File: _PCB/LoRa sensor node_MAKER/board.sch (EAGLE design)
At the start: 25 parts

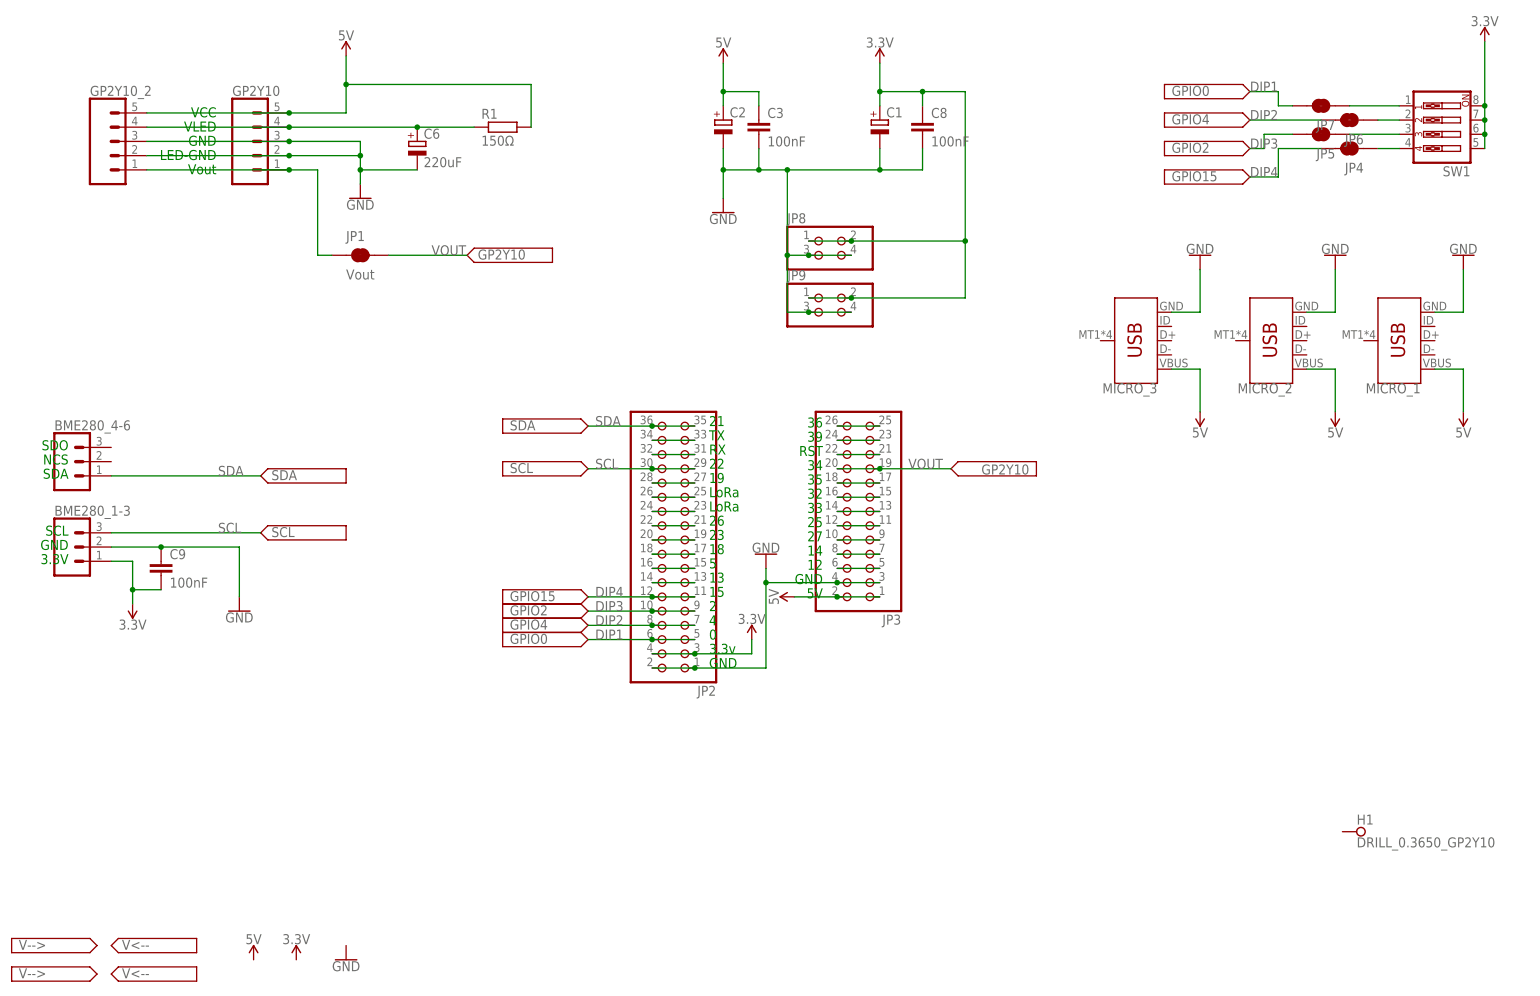
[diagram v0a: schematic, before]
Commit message: CH340E converter complete + LoRa sensor node
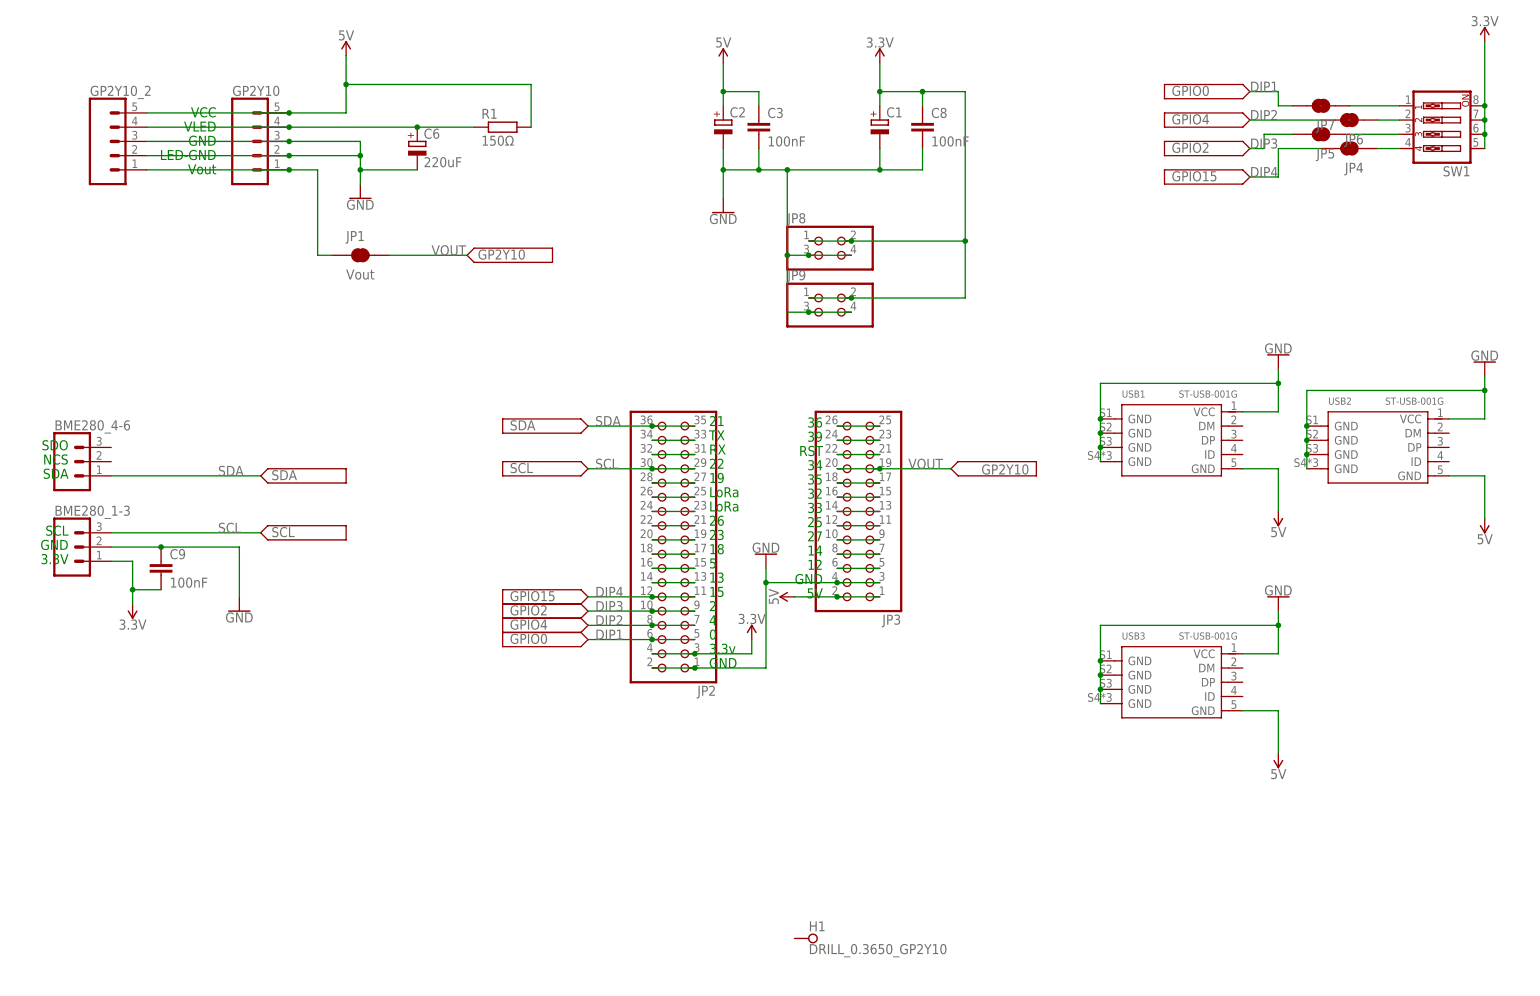
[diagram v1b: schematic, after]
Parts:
- removed MICRO_1, MICRO_2, MICRO_3: (no value), SparkFun-Connectors:USB_MICRO-B_SMT
- added USB1, USB2, USB3: ST-USB-001G, Seeed-Connector:MICRO-USB-SMD-B-WITHOUT-POST-W/P(ST-USB-001G)
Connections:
- net 5V: now also USB1.GND@5, USB2.GND@5, USB3.GND@5; no longer MICRO_1.VBUS, MICRO_2.VBUS, MICRO_3.VBUS
- net GND: now also USB1.GND@1, USB1.GND@2, USB1.GND@3, USB1.GND@4, USB1.VCC, USB2.GND@1, USB2.GND@2, USB2.GND@3, USB2.GND@4, USB2.VCC, USB3.GND@1, USB3.GND@2, USB3.GND@3, USB3.GND@4, USB3.VCC; no longer MICRO_1.GND, MICRO_2.GND, MICRO_3.GND
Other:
- moved on the sheet: H1

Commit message: error correciton
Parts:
- removed USB1: ST-USB-001G, Seeed-Connector:MICRO-USB-SMD-B-WITHOUT-POST-W/P(ST-USB-001G)
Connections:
- net 5V: no longer USB1.GND@5
- net GND: no longer USB1.GND@1, USB1.GND@2, USB1.GND@3, USB1.GND@4, USB1.VCC
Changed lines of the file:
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@@
 <setting verticaltext="up"/>
 </settings>
-<grid distance="50" unitdist="mil" unit="mil" style="lines" multiple="1" display="no" altdistance="0.01" altunitdist="inch" altunit="inch"/>
+<grid distance="0.1" unitdist="inch" unit="inch" style="lines" multiple="1" display="no" altdistance="0.01" altunitdist="inch" altunit="inch"/>
 <layers>
 <layer number="1" name="Top" color="4" fill="1" visible="no" active="no"/>
@@
 <part name="JP8" library="pinhead_v2" deviceset="PINHD-2X2" device="/OCT"/>
 <part name="JP9" library="pinhead_v2" deviceset="PINHD-2X2" device="/OCT"/>
-<part name="USB1" library="Seeed-Connector" library_urn="urn:adsk.eagle:library:478" deviceset="MICRO-USB-SMD-B-WITHOUT-POST-W/P(ST-USB-001G)" device="" package3d_urn="urn:adsk.eagle:package:33109/1" value="ST-USB-001G"/>
-<part name="SUPPLY17" library="SparkFun-PowerSymbols" library_urn="urn:adsk.eagle:library:530" deviceset="5V" device=""/>
-<part name="GND9" library="SparkFun-PowerSymbols" library_urn="urn:adsk.eagle:library:530" deviceset="GND" device=""/>
 <part name="USB2" library="Seeed-Connector" library_urn="urn:adsk.eagle:library:478" deviceset="MICRO-USB-SMD-B-WITHOUT-POST-W/P(ST-USB-001G)" device="" package3d_urn="urn:adsk.eagle:package:33109/1" value="ST-USB-001G"/>
 <part name="SUPPLY32" library="SparkFun-PowerSymbols" library_urn="urn:adsk.eagle:library:530" deviceset="5V" device=""/>
@@
 <attribute name="VALUE" x="146.05" y="120.65" size="1.778" layer="96"/>
 </instance>
-<instance part="USB1" gate="USB" x="214.63" y="102.87" smashed="yes">
-<attribute name="NAME" x="205.74" y="110.49" size="1.27" layer="95" ratio="10"/>
-<attribute name="VALUE" x="215.9" y="110.49" size="1.27" layer="95" ratio="10"/>
-</instance>
-<instance part="SUPPLY17" gate="G$1" x="233.68" y="90.17" smashed="yes" rot="R180">
-<attribute name="VALUE" x="233.68" y="87.376" size="1.778" layer="96" rot="R180" align="bottom-center"/>
-</instance>
-<instance part="GND9" gate="1" x="233.68" y="118.11" smashed="yes" rot="R180">
-<attribute name="VALUE" x="233.68" y="118.364" size="1.778" layer="96" rot="R180" align="top-center"/>
-</instance>
 <instance part="USB2" gate="USB" x="251.46" y="101.6" smashed="yes">
 <attribute name="NAME" x="242.57" y="109.22" size="1.27" layer="95" ratio="10"/>
@@
 </segment>
 <segment>
-<pinref part="GND9" gate="1" pin="GND"/>
-<wire x1="227.33" y1="107.95" x2="233.68" y2="107.95" width="0.1524" layer="91"/>
-<wire x1="233.68" y1="107.95" x2="233.68" y2="113.03" width="0.1524" layer="91"/>
-<pinref part="USB1" gate="USB" pin="VCC"/>
-<pinref part="USB1" gate="USB" pin="GND@4"/>
-<pinref part="USB1" gate="USB" pin="GND@3"/>
-<wire x1="233.68" y1="113.03" x2="233.68" y2="115.57" width="0.1524" layer="91"/>
-<wire x1="201.93" y1="99.06" x2="201.93" y2="101.6" width="0.1524" layer="91"/>
-<pinref part="USB1" gate="USB" pin="GND@2"/>
-<wire x1="201.93" y1="101.6" x2="201.93" y2="104.14" width="0.1524" layer="91"/>
-<junction x="201.93" y="101.6"/>
-<pinref part="USB1" gate="USB" pin="GND@1"/>
-<wire x1="201.93" y1="104.14" x2="201.93" y2="106.68" width="0.1524" layer="91"/>
-<junction x="201.93" y="104.14"/>
-<wire x1="201.93" y1="106.68" x2="201.93" y2="113.03" width="0.1524" layer="91"/>
-<wire x1="201.93" y1="113.03" x2="233.68" y2="113.03" width="0.1524" layer="91"/>
-<junction x="201.93" y="106.68"/>
-<junction x="233.68" y="113.03"/>
-</segment>
-<segment>
 <pinref part="GND10" gate="1" pin="GND"/>
 <wire x1="264.16" y1="106.68" x2="270.51" y2="106.68" width="0.1524" layer="91"/>
@@
 </segment>
 <segment>
-<pinref part="SUPPLY17" gate="G$1" pin="5V"/>
-<wire x1="227.33" y1="97.79" x2="233.68" y2="97.79" width="0.1524" layer="91"/>
-<wire x1="233.68" y1="97.79" x2="233.68" y2="90.17" width="0.1524" layer="91"/>
-<pinref part="USB1" gate="USB" pin="GND@5"/>
-</segment>
-<segment>

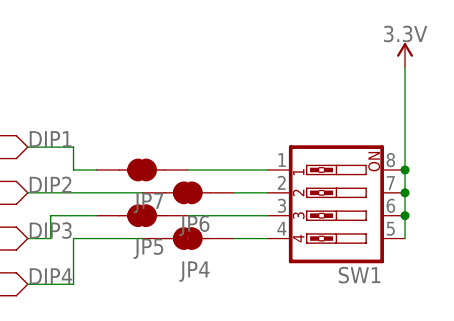
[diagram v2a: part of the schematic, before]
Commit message: LoRa sensor node PCB update
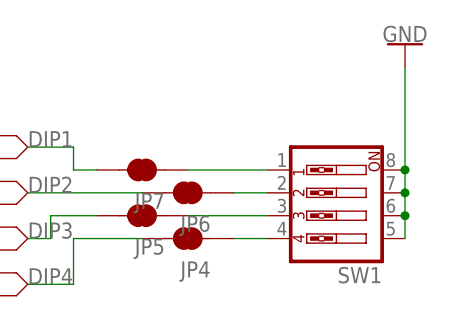
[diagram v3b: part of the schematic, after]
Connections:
- net 3.3V: no longer SW1.5, SW1.6, SW1.7, SW1.8
- net GND: now also SW1.5, SW1.6, SW1.7, SW1.8
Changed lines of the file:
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@@
 <setting verticaltext="up"/>
 </settings>
-<grid distance="0.1" unitdist="inch" unit="inch" style="lines" multiple="1" display="no" altdistance="0.01" altunitdist="inch" altunit="inch"/>
+<grid distance="0.05" unitdist="inch" unit="inch" style="lines" multiple="1" display="no" altdistance="0.01" altunitdist="inch" altunit="inch"/>
 <layers>
 <layer number="1" name="Top" color="4" fill="1" visible="no" active="no"/>
@@
 <part name="JP6" library="SparkFun-Jumpers" library_urn="urn:adsk.eagle:library:528" deviceset="JUMPER-SMT_2_NC_TRACE" device="_SILK" package3d_urn="urn:adsk.eagle:package:39281/1" value=""/>
 <part name="JP7" library="SparkFun-Jumpers" library_urn="urn:adsk.eagle:library:528" deviceset="JUMPER-SMT_2_NC_TRACE" device="_SILK" package3d_urn="urn:adsk.eagle:package:39281/1" value=""/>
-<part name="SUPPLY2" library="SparkFun-PowerSymbols" library_urn="urn:adsk.eagle:library:530" deviceset="3.3V" device=""/>
 <part name="SUPPLY18" library="supply2" library_urn="urn:adsk.eagle:library:372" deviceset="V--&gt;" device="" value="GPIO15"/>
 <part name="SUPPLY19" library="supply2" library_urn="urn:adsk.eagle:library:372" deviceset="V--&gt;" device="" value="GPIO2"/>
@@
 <part name="SUPPLY33" library="SparkFun-PowerSymbols" library_urn="urn:adsk.eagle:library:530" deviceset="5V" device=""/>
 <part name="GND11" library="SparkFun-PowerSymbols" library_urn="urn:adsk.eagle:library:530" deviceset="GND" device=""/>
+<part name="GND3" library="SparkFun-PowerSymbols" library_urn="urn:adsk.eagle:library:530" deviceset="GND" device=""/>
 </parts>
 <sheets>
@@
 <attribute name="VALUE" x="243.84" y="165.1" size="1.778" layer="96" font="vector" rot="R180" align="top-left"/>
 </instance>
-<instance part="SUPPLY2" gate="G$1" x="270.51" y="173.99" smashed="yes">
-<attribute name="VALUE" x="270.51" y="176.784" size="1.778" layer="96" align="bottom-center"/>
-</instance>
 <instance part="SUPPLY18" gate="G$1" x="213.36" y="149.86" smashed="yes">
 <attribute name="VALUE" x="214.63" y="149.098" size="1.778" layer="96"/>
@@
 <instance part="GND11" gate="1" x="233.68" y="74.93" smashed="yes" rot="R180">
 <attribute name="VALUE" x="233.68" y="75.184" size="1.778" layer="96" rot="R180" align="top-center"/>
+</instance>
+<instance part="GND3" gate="1" x="270.51" y="176.53" smashed="yes" rot="R180">
+<attribute name="VALUE" x="270.51" y="176.784" size="1.778" layer="96" rot="R180" align="top-center"/>
 </instance>
 </instances>
@@
 <junction x="233.68" y="69.85"/>
 </segment>
+<segment>
+<pinref part="SW1" gate="A" pin="8"/>
+<pinref part="SW1" gate="A" pin="7"/>
+<wire x1="270.51" y1="160.02" x2="270.51" y2="162.56" width="0.1524" layer="91"/>
+<junction x="270.51" y="160.02"/>
+<pinref part="SW1" gate="A" pin="6"/>
+<wire x1="270.51" y1="157.48" x2="270.51" y2="160.02" width="0.1524" layer="91"/>
+<junction x="270.51" y="157.48"/>
+<pinref part="SW1" gate="A" pin="5"/>
+<wire x1="270.51" y1="154.94" x2="270.51" y2="157.48" width="0.1524" layer="91"/>
+<wire x1="270.51" y1="162.56" x2="270.51" y2="173.99" width="0.1524" layer="91"/>
+<junction x="270.51" y="162.56"/>
+<pinref part="GND3" gate="1" pin="GND"/>
+</segment>
 </net>
 <net name="5V" class="1">
@@
 <junction x="29.21" y="76.2"/>
 </segment>
-<segment>
-<pinref part="SW1" gate="A" pin="8"/>
-<pinref part="SW1" gate="A" pin="7"/>
-<wire x1="270.51" y1="160.02" x2="270.51" y2="162.56" width="0.1524" layer="91"/>
-<junction x="270.51" y="160.02"/>
-<pinref part="SW1" gate="A" pin="6"/>
-<wire x1="270.51" y1="157.48" x2="270.51" y2="160.02" width="0.1524" layer="91"/>
-<junction x="270.51" y="157.48"/>
-<pinref part="SW1" gate="A" pin="5"/>
-<wire x1="270.51" y1="154.94" x2="270.51" y2="157.48" width="0.1524" layer="91"/>
-<pinref part="SUPPLY2" gate="G$1" pin="3.3V"/>
-<wire x1="270.51" y1="162.56" x2="270.51" y2="173.99" width="0.1524" layer="91"/>
-<junction x="270.51" y="162.56"/>
-</segment>
-</net>
+</net>
